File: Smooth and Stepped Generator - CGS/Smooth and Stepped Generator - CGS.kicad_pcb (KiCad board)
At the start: 2 copper layers, 112 parts, among them J1 IN_A, J10 LA_A, J11 LK_A, J12 OUT_B, J13 CYCLE_B, J14 CYCLE_A, J15 COUPLER, J16 CA, J17 CK, J18 RD_OUT, J19 +12V_Conn, J2 IN_B, J20 GND_Conn, J21 -12V_Conn, J22 RATE_A, J23 RATE_B, J3 VC_A, J4 VC_B, J5 HOLD_A, J6 SAMPLE, J7 LA_B, J8 LK_B, J9 OUT_A, Q1 2N3906, Q2 2N3906, Q3 Q_NJFET_GDS, Q4 Q_NJFET_GDS, U1 LM3900, U2 CA3080, U3 CA3080, U4 TL072, U5 TL072, U7 LM741, U8 LM3900

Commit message: lots of stuff tbh
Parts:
- moved R12 7.94 mm to (7.49, 5.87), turned to 160 degrees
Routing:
- net Net-(D1-Pad1): track 12.0 -> 0.00 mm
- net Net-(C1-Pad1): track 11.9 -> 0.00 mm
- net Net-(D1-Pad2): track 11.6 -> 0.00 mm
- net Net-(Q1-Pad3): track 11.3 -> 0.00 mm
- net Net-(Q1-Pad1): track 9.18 -> 0.00 mm
- net Net-(J1-Pad1): track 8.23 -> 0.00 mm
- net Net-(R15-Pad1): track 7.31 -> 0.00 mm
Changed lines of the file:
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@@
     (thickness 1.6)
     (drawings 0)
-    (tracks 20)
+    (tracks 2)
     (zones 0)
     (modules 112)
@@
   (setup
     (last_trace_width 0.25)
+    (user_trace_width 0.4064)
+    (user_trace_width 0.8128)
     (trace_clearance 0.2)
     (zone_clearance 0.508)
@@
     (solder_mask_min_width 0.25)
     (aux_axis_origin 0 0)
-    (visible_elements FFFFF77F)
+    (visible_elements FFFFFF7F)
     (pcbplotparams
       (layerselection 0x010fc_ffffffff)
@@
   )
   (module Resistor_THT:R_Axial_DIN0207_L6.3mm_D2.5mm_P7.62mm_Horizontal (layer F.Cu)
-    (at 11.895401 -0.736399)
+    (at 7.493 5.8674 160)
     (descr "Resistor, Axial_DIN0207 series, Axial, Horizontal, pin pitch=7.62mm, 0.25W = 1/4W, length*diameter=6.3*2.5mm^2, http://cdn-reichelt.de/documents/datenblatt/B400/1_4W%23YAG.pdf")
     (tags "Resistor Axial_DIN0207 series Axial Horizontal pin pitch 7.62mm 0.25W = 1/4W length 6.3mm diameter 2.5mm")
-    (fp_text reference R12 (at 3.81 -2.37) (layer F.SilkS)
+    (fp_text reference R12 (at 3.81 -2.37 160) (layer F.SilkS)
       (effects (font (size 1 1) (thickness 0.15)))
     )
-    (fp_text value 15K (at 3.81 2.37) (layer F.Fab)
+    (fp_text value 15K (at 3.81 2.37 160) (layer F.Fab)
       (effects (font (size 1 1) (thickness 0.15)))
     )
@@
     (fp_line (start 8.67 1.5) (end 8.67 -1.5) (layer F.CrtYd) (width 0.05))
     (fp_line (start 8.67 -1.5) (end -1.05 -1.5) (layer F.CrtYd) (width 0.05))
-    (fp_text user %R (at 3.81 0) (layer F.Fab)
+    (fp_text user %R (at 3.81 0 160) (layer F.Fab)
       (effects (font (size 1 1) (thickness 0.15)))
     )
-    (pad 1 thru_hole circle (at 0 0) (size 1.6 1.6) (drill 0.8) (layers *.Cu *.Mask)
+    (pad 1 thru_hole circle (at 0 0 160) (size 1.6 1.6) (drill 0.8) (layers *.Cu *.Mask)
       (net 41 "Net-(Q2-Pad1)"))
-    (pad 2 thru_hole oval (at 7.62 0) (size 1.6 1.6) (drill 0.8) (layers *.Cu *.Mask)
+    (pad 2 thru_hole oval (at 7.62 0 160) (size 1.6 1.6) (drill 0.8) (layers *.Cu *.Mask)
       (net 1 Earth))
     (model ${KISYS3DMOD}/Resistor_THT.3dshapes/R_Axial_DIN0207_L6.3mm_D2.5mm_P7.62mm_Horizontal.wrl
@@
     )
   )
-  (segment (start 38.014336 31.35302) (end 40.8432 34.8234) (width 0.25) (layer B.Cu) (net 2))
-  (segment (start 38.014336 31.35302) (end 34.9758 30.6578) (width 0.25) (layer B.Cu) (net 2))
-  (segment (start 34.9758 30.6578) (end 31.8262 33.655) (width 0.25) (layer B.Cu) (net 2))
-  (segment (start 26.7716 24.5364) (end 29.114849 22.543424) (width 0.25) (layer B.Cu) (net 16))
-  (segment (start 26.881207 19.841958) (end 29.114849 22.543424) (width 0.25) (layer B.Cu) (net 16))
-  (segment (start 33.116294 25.515761) (end 29.114849 22.543424) (width 0.25) (layer B.Cu) (net 16))
-  (segment (start 30.772713 16.576597) (end 33.006355 19.278063) (width 0.25) (layer B.Cu) (net 17))
-  (segment (start 34.735965 16.258399) (end 33.006355 19.278063) (width 0.25) (layer B.Cu) (net 17))
-  (segment (start 35.062047 23.883081) (end 33.006355 19.278063) (width 0.25) (layer B.Cu) (net 17))
-  (segment (start 17.7292 33.909) (end 16.5862 29.6418) (width 0.25) (layer B.Cu) (net 24))
-  (segment (start 20.172486 28.3464) (end 16.5862 29.6418) (width 0.25) (layer B.Cu) (net 24))
   (segment (start 15.2654 47.625) (end 15.3924 44.3484) (width 0.25) (layer B.Cu) (net 28))
-  (segment (start 22.733 40.9448) (end 19.2532 36.9316) (width 0.25) (layer B.Cu) (net 38))
-  (segment (start 15.3924 36.7284) (end 19.2532 36.9316) (width 0.25) (layer B.Cu) (net 38))
-  (segment (start 25.908 44.6278) (end 25.234412 40.503734) (width 0.25) (layer B.Cu) (net 39))
-  (segment (start 25.908 44.6278) (end 29.087158 42.718059) (width 0.25) (layer B.Cu) (net 39))
-  (segment (start 31.677958 44.877059) (end 29.087158 42.718059) (width 0.25) (layer B.Cu) (net 39))
-  (segment (start 33.9852 36.8808) (end 36.068583 32.9857) (width 0.25) (layer B.Cu) (net 49))
-  (segment (start 37.6428 35.4076) (end 36.068583 32.9857) (width 0.25) (layer B.Cu) (net 49))
   (segment (start 15.2654 51.689) (end 19.308886 48.4378) (width 0.25) (layer B.Cu) (net 83))
 )

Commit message: ssg work
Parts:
- removed the REF** at (120.4, 103.4)
- removed the REF** at (152.7, 20.9)
- removed the REF** at (20.1, 93.5)
- added REF**: MountingHole_3.5mm_Pad, MountingHole:MountingHole_3.5mm_Pad, F.Cu at (120.3, 17.7)
- added REF**: MountingHole_3.5mm_Pad, MountingHole:MountingHole_3.5mm_Pad, F.Cu at (120.1, 70.0)
- added REF**: MountingHole_3.5mm_Pad, MountingHole:MountingHole_3.5mm_Pad, F.Cu at (17.7, 70.0)
- D8: footprint Connector_Wire:SolderWirePad_1x01_Drill1mm -> Diode_THT:D_T-1_P5.08mm_Horizontal
- J18: footprint Connector_Wire:SolderWirePad_1x02_P3.81mm_Drill1mm -> Connector_Wire:SolderWirePad_1x01_Drill1mm
- moved U7 135.2 mm to (114.3, 49.3), turned to 310 degrees
- moved J11 126.5 mm to (39.1, 53.2), turned to 330 degrees
- moved U8 123.1 mm to (102.6, 32.3), turned to 280 degrees
- moved R50 116.9 mm to (109.7, 67.4), turned to 40 degrees
- moved R26 116.4 mm to (99.8, 56.3), turned to 140 degrees
- moved U4 114.4 mm to (20.3, 61.9), turned to 50 degrees
- moved J8 114.0 mm to (26.1, 49.0), turned to 50 degrees
- moved R24 113.8 mm to (97.8, 59.0), turned to 250 degrees
- moved D4 113.6 mm to (73.8, 58.8), turned to 70 degrees
- moved R51 111.2 mm to (101.6, 58.7), turned to 290 degrees
- moved U3 110.9 mm to (82.4, 54.7), turned to 340 degrees
- moved R54 108.0 mm to (116.8, 47.1), turned to 310 degrees
- moved R55 107.7 mm to (117.3, 42.3), turned to 310 degrees
- moved R39 105.8 mm to (26.7, 53.7), turned to 50 degrees
- moved J10 104.4 mm to (50.8, 38.9), turned to 330 degrees
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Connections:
- R13 pad 2: Net-(R13-Pad2) -> Net-(J3-Pad1)
- R14 pad 2: Net-(R14-Pad2) -> Net-(J4-Pad1)
- R7 pad 1: Net-(R13-Pad2) -> Net-(J3-Pad1)
- R8 pad 1: Net-(R14-Pad2) -> Net-(J4-Pad1)
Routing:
- net +12V: track 0.00 -> 280.0 mm
- net Earth: track 0.00 -> 280.0 mm
- net -12V: track 0.00 -> 231.8 mm
- net Net-(J9-Pad1): track 0.00 -> 99.0 mm, vias 0 -> 1
- net Net-(R28-Pad1): track 0.00 -> 73.3 mm
- net Sample: track 0.00 -> 54.8 mm, vias 0 -> 1
- net Net-(R17-Pad1): track 0.00 -> 48.4 mm
- net Net-(Q1-Pad3): track 0.00 -> 48.1 mm, vias 0 -> 1
- net Net-(J12-Pad1): track 0.00 -> 47.9 mm
- net Net-(R33-Pad1): track 0.00 -> 46.2 mm
- net Net-(C4-Pad2): track 0.00 -> 44.7 mm
- net Net-(R36-Pad1): track 0.00 -> 38.2 mm
- net Net-(R21-Pad2): track 0.00 -> 30.8 mm
- net Net-(D7-Pad1): track 0.00 -> 28.9 mm
- net Net-(R24-Pad2): track 0.00 -> 28.1 mm
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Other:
- board outline added: 113.5 x 63.5 mm

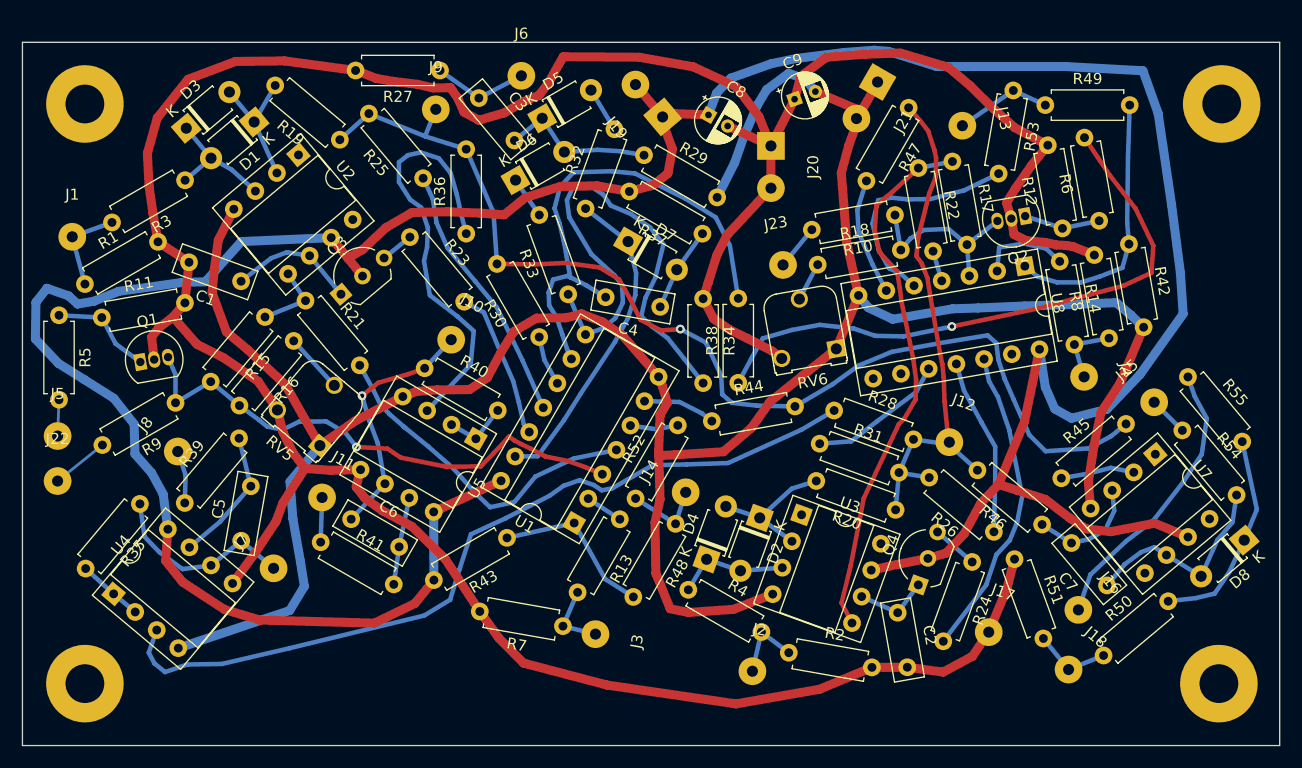
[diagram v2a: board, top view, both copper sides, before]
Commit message: cleaned up ssg silkscreen
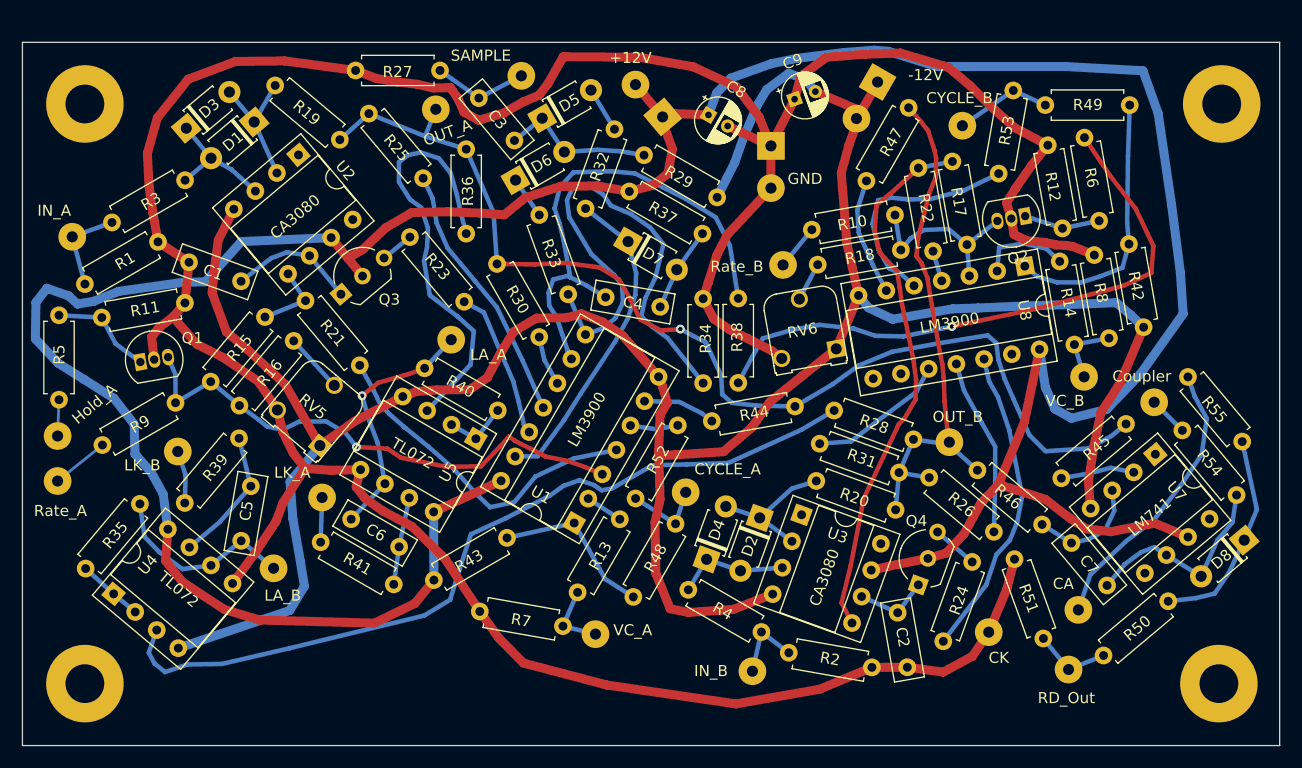
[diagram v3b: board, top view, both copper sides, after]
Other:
- board text added: "+12V"
- board text added: "-12V"
- board text added: "CA"
- board text added: "CA3080"
- board text added: "CK"
- board text added: "CYCLE_A"
- board text added: "CYCLE_B"
- board text added: "Coupler"
- board text added: "GND"
- board text added: "Hold_A"
- board text added: "IN_A"
- board text added: "IN_B"
- board text added: "LA_A"
- board text added: "LA_B"
- board text added: "LK_A"
- board text added: "LK_B"
- board text added: "LM3900"
- board text added: "LM741"
- board text added: "OUT_A"
- board text added: "OUT_B"
- board text added: "RD_Out"
- board text added: "Rate_A"
- board text added: "Rate_B"
- board text added: "SAMPLE"
- board text added: "TL072"
- board text added: "VC_A"
- board text added: "VC_B"

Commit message: literally so much stuff
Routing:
- added copper zone on B.Cu, net Earth
- added copper zone on F.Cu, net Earth
